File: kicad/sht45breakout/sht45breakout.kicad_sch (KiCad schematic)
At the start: 3 parts, among them J1 Conn_01x04, U1 SHT4x

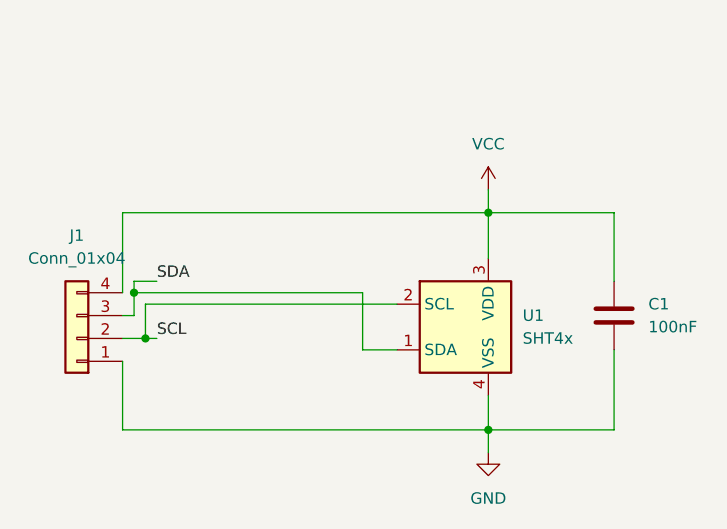
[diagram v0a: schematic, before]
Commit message: add 4.7k pullup resistors and solder jumpers to enable them (by default they are disabled)
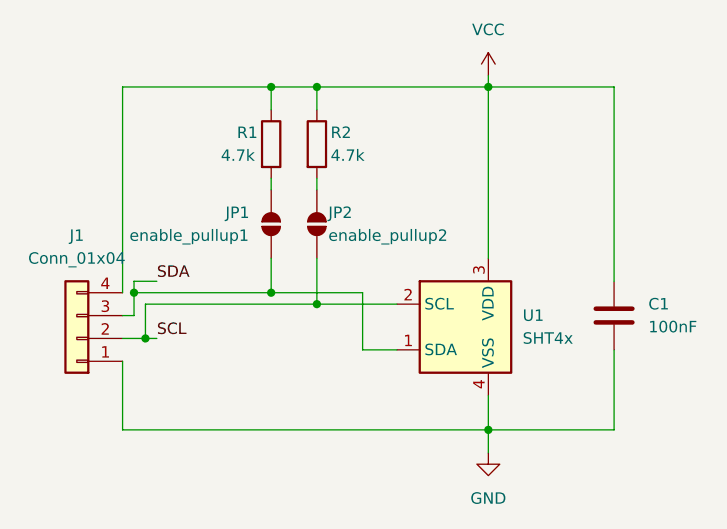
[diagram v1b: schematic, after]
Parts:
- added JP1: enable_pullup1, Jumper:SolderJumper-2_P1.3mm_Open_TrianglePad1.0x1.5mm, symbol Jumper:SolderJumper_2_Open
- added JP2: enable_pullup2, Jumper:SolderJumper-2_P1.3mm_Open_TrianglePad1.0x1.5mm, symbol Jumper:SolderJumper_2_Open
- added R1, R2: 4.7k, foxisfrickellibrary:R_0402_modsilkscreen, symbol Device:R
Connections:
- net SCL: now also JP2.1 (A)
- net SDA: now also JP1.1 (A)
- net VCC: now also R1.1, R2.1
- new net: JP2.2 (B), R2.2
- new net: JP1.2 (B), R1.2
